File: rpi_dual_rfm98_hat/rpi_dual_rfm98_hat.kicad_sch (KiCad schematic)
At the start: 19 parts, among them J1 Conn_01x02_Male, J2 Conn_Coaxial, J3 Conn_Coaxial, J4 Conn_01x03_Male, P1 Conn_02x20_Odd_Even, U1 RFM98PW-symbols, U2 RFM98PW-symbols

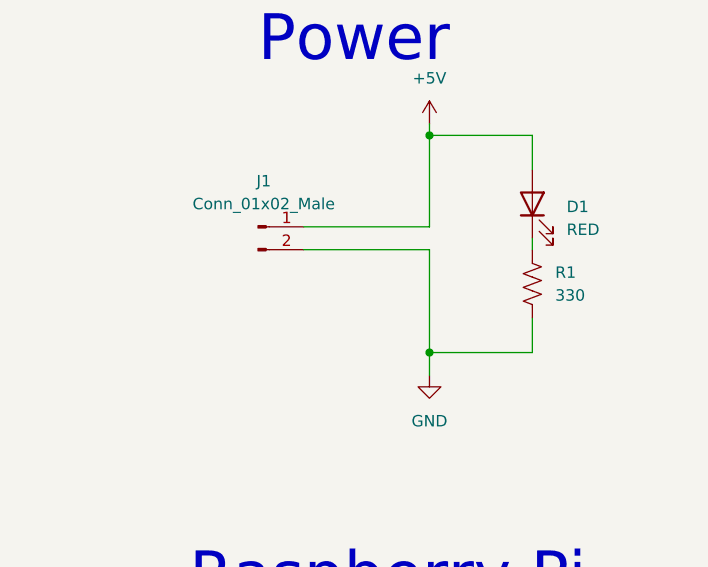
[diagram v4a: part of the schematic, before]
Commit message: Added the fan connector
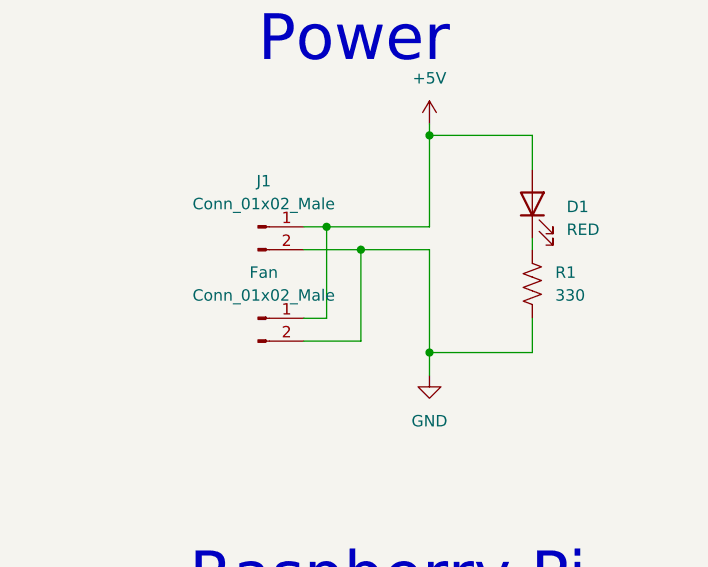
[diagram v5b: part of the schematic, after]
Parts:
- added Fan: Conn_01x02_Male, Connector_PinHeader_2.54mm:PinHeader_1x02_P2.54mm_Vertical, symbol Connector:Conn_01x02_Male
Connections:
- net +5V: now also Fan.1 (Pin_1)
- net GND: now also Fan.2 (Pin_2)
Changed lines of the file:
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@@
   (junction (at 71.12 137.16) (diameter 1.016) (color 0 0 0 0)
   )
+  (junction (at 54.61 44.45) (diameter 0) (color 0 0 0 0)
+  )
   (junction (at 62.23 31.75) (diameter 0) (color 0 0 0 0)
   )
@@
   )
   (junction (at 200.66 96.52) (diameter 0) (color 0 0 0 0)
+  )
+  (junction (at 50.8 41.91) (diameter 0) (color 0 0 0 0)
   )
   (junction (at 71.12 119.38) (diameter 1.016) (color 0 0 0 0)
@@
     (stroke (width 0) (type solid) (color 0 0 0 0))
   )
+  (wire (pts (xy 50.8 52.07) (xy 50.8 41.91))
+    (stroke (width 0) (type default) (color 0 0 0 0))
+  )
   (wire (pts (xy 200.66 83.82) (xy 200.66 96.52))
     (stroke (width 0) (type default) (color 0 0 0 0))
@@
     (stroke (width 0) (type solid) (color 0 0 0 0))
   )
+  (wire (pts (xy 54.61 54.61) (xy 54.61 44.45))
+    (stroke (width 0) (type default) (color 0 0 0 0))
+  )
   (wire (pts (xy 53.34 127) (xy 53.34 144.78))
     (stroke (width 0) (type solid) (color 0 0 0 0))
   )
-  (wire (pts (xy 48.26 44.45) (xy 62.23 44.45))
+  (wire (pts (xy 48.26 44.45) (xy 54.61 44.45))
     (stroke (width 0) (type default) (color 0 0 0 0))
   )
@@
     (stroke (width 0) (type default) (color 0 0 0 0))
   )
+  (wire (pts (xy 48.26 54.61) (xy 54.61 54.61))
+    (stroke (width 0) (type default) (color 0 0 0 0))
+  )
   (wire (pts (xy 144.78 91.44) (xy 160.02 91.44))
     (stroke (width 0) (type default) (color 0 0 0 0))
@@
     (stroke (width 0) (type default) (color 0 0 0 0))
   )
+  (wire (pts (xy 48.26 52.07) (xy 50.8 52.07))
+    (stroke (width 0) (type default) (color 0 0 0 0))
+  )
   (wire (pts (xy 71.12 101.6) (xy 71.12 111.76))
     (stroke (width 0) (type solid) (color 0 0 0 0))
@@
     (stroke (width 0) (type default) (color 0 0 0 0))
   )
-  (wire (pts (xy 48.26 41.91) (xy 62.23 41.91))
+  (wire (pts (xy 48.26 41.91) (xy 50.8 41.91))
     (stroke (width 0) (type default) (color 0 0 0 0))
   )
@@
     (stroke (width 0) (type default) (color 0 0 0 0))
   )
+  (wire (pts (xy 50.8 41.91) (xy 62.23 41.91))
+    (stroke (width 0) (type default) (color 0 0 0 0))
+  )
   (wire (pts (xy 226.06 38.1) (xy 226.06 40.64))
     (stroke (width 0) (type default) (color 0 0 0 0))
@@
   (wire (pts (xy 73.66 92.71) (xy 73.66 96.52))
     (stroke (width 0) (type solid) (color 0 0 0 0))
+  )
+  (wire (pts (xy 54.61 44.45) (xy 62.23 44.45))
+    (stroke (width 0) (type default) (color 0 0 0 0))
   )
   (wire (pts (xy 132.08 68.58) (xy 132.08 72.39))
@@
     (pin "3")
   )
+  (symbol (lib_id "Connector:Conn_01x02_Male") (at 43.18 52.07 0) (unit 1)
+    (in_bom yes) (on_board yes) (fields_autoplaced)
+    (property "Reference" "Fan" (id 0) (at 43.815 46.99 0))
+    (property "Value" "Conn_01x02_Male" (id 1) (at 43.815 49.53 0))
+    (property "Footprint" "Connector_PinHeader_2.54mm:PinHeader_1x02_P2.54mm_Vertical" (id 2) (at 43.18 52.07 0)
+      (effects (font (size 1.27 1.27)) hide)
+    )
+    (property "Datasheet" "~" (id 3) (at 43.18 52.07 0)
+      (effects (font (size 1.27 1.27)) hide)
+    )
+    (pin "1")
+    (pin "2")
+  )
   (symbol (lib_id "power:GND") (at 200.66 99.06 0) (unit 1)
     (in_bom yes) (on_board yes) (fields_autoplaced)
@@
       (reference "D3") (unit 1) (value "GREEN") (footprint "LED_SMD:LED_0603_1608Metric")
     )
+    (path "/ce7482e9-86e5-4ff0-9c5b-7d710b908922"
+      (reference "Fan") (unit 1) (value "Conn_01x02_Male") (footprint "Connector_PinHeader_2.54mm:PinHeader_1x02_P2.54mm_Vertical")
+    )
     (path "/ef12ae7e-a55f-475d-abf0-059cecf4d950"
